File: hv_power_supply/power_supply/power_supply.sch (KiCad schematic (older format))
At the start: 0 parts

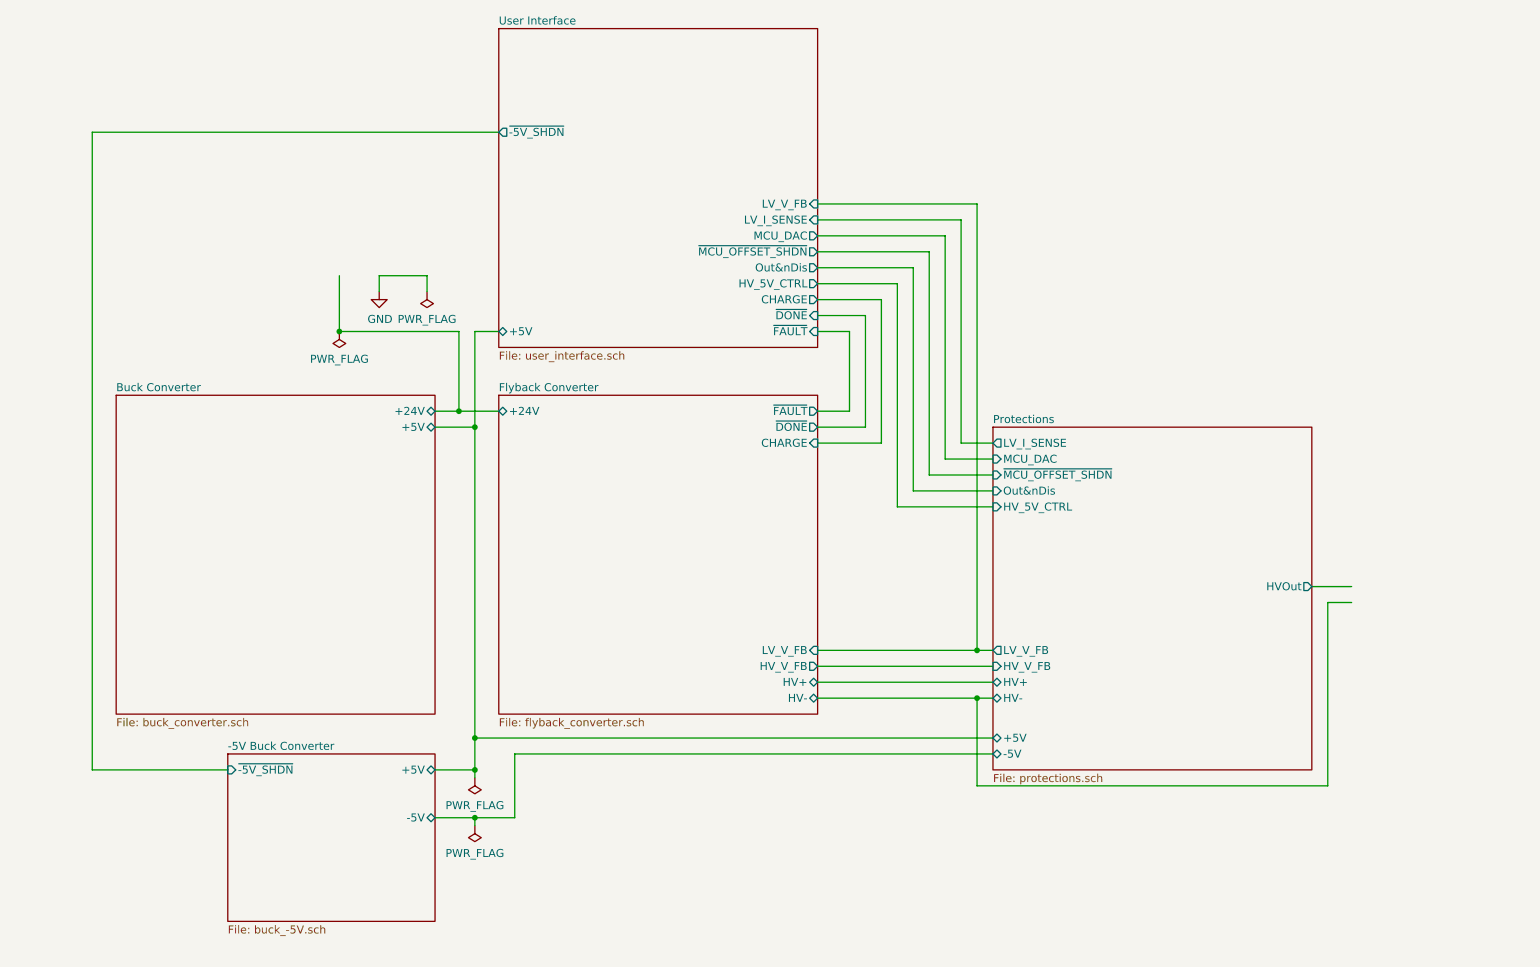
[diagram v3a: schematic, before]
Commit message: Fixed all component footprint issues, beginning to lay out flyback portion
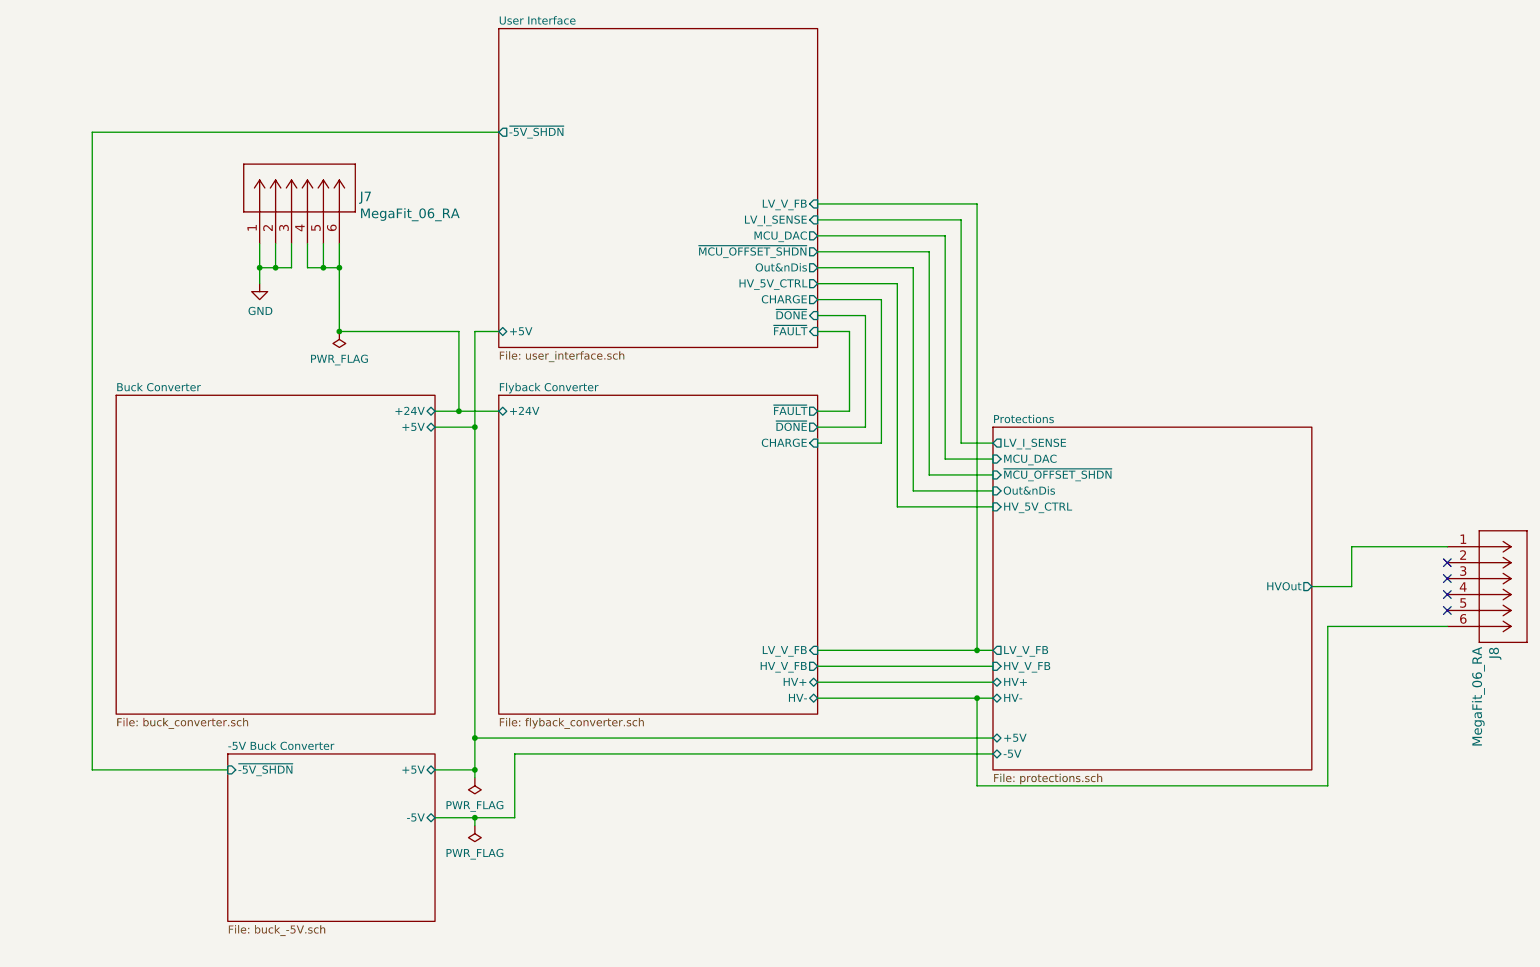
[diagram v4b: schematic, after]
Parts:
- added J7, J8: MegaFit_06_RA, footprints:MegaFit_06_RA, symbol formula:MegaFit_06_RA
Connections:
- wire segments 61 -> 71
- no-connect marks 0 -> 4
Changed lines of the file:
@@
 	7200 4950 7300 4950
-Wire Wire Line
-	9400 4350 9550 4350
 Wire Wire Line
 	9300 4250 9550 4250
@@
 L power:GND #PWR01
 U 1 1 607CC6CE
-P 3450 2400
-F 0 "#PWR01" H 3450 2150 50  0001 C CNN
-F 1 "GND" H 3455 2227 50  0000 C CNN
-F 2 "" H 3450 2400 50  0001 C CNN
-F 3 "" H 3450 2400 50  0001 C CNN
-	1    3450 2400
+P 2700 2350
+F 0 "#PWR01" H 2700 2100 50  0001 C CNN
+F 1 "GND" H 2705 2177 50  0000 C CNN
+F 2 "" H 2700 2350 50  0001 C CNN
+F 3 "" H 2700 2350 50  0001 C CNN
+	1    2700 2350
 	1    0    0    -1
 $EndComp
@@
 Connection ~ 3200 2650
 $Comp
-L power:PWR_FLAG #FLG02
+L power:PWR_FLAG #FLG03
 U 1 1 605FBEF3
 P 4050 5450
-F 0 "#FLG02" H 4050 5525 50  0001 C CNN
+F 0 "#FLG03" H 4050 5525 50  0001 C CNN
 F 1 "PWR_FLAG" H 4050 5623 50  0000 C CNN
 F 2 "" H 4050 5450 50  0001 C CNN
@@
 	4050 5400 4050 5450
 $Comp
-L power:PWR_FLAG #FLG03
+L power:PWR_FLAG #FLG04
 U 1 1 605FB304
 P 4050 5750
-F 0 "#FLG03" H 4050 5825 50  0001 C CNN
+F 0 "#FLG04" H 4050 5825 50  0001 C CNN
 F 1 "PWR_FLAG" H 4050 5923 50  0000 C CNN
 F 2 "" H 4050 5750 50  0001 C CNN
@@
 	7200 4950 7200 5500
 Wire Wire Line
-	9400 4350 9400 5500
-Wire Wire Line
 	4300 5700 4300 5300
 Wire Wire Line
 	4300 5300 7300 5300
-$Comp
-L power:PWR_FLAG #FLG0101
-U 1 1 6063E536
-P 3750 2400
-F 0 "#FLG0101" H 3750 2475 50  0001 C CNN
-F 1 "PWR_FLAG" H 3750 2573 50  0000 C CNN
-F 2 "" H 3750 2400 50  0001 C CNN
-F 3 "" H 3750 2400 50  0001 C CNN
-	1    3750 2400
-	-1   0    0    1
-$EndComp
-Wire Wire Line
-	3450 2400 3450 2300
-Wire Wire Line
-	3450 2300 3750 2300
-Wire Wire Line
-	3750 2300 3750 2400
-Wire Wire Line
-	3200 2300 3200 2650
+Wire Wire Line
+	2700 2350 2700 2250
 Wire Wire Line
 	6200 2250 6800 2250
@@
 Wire Wire Line
 	1650 1400 4200 1400
+$Comp
+L formula:MegaFit_06_RA J7
+U 1 1 60636060
+P 2700 2100
+F 0 "J7" V 2995 1472 60  0000 R CNN
+F 1 "MegaFit_06_RA" V 2889 1472 60  0000 R CNN
+F 2 "footprints:MegaFit_06_RA" H 3100 1840 60  0001 C CNN
+F 3 "https://www.molex.com/pdm_docs/as/AS-76823-100.pdf" H 2700 2100 60  0001 C CNN
+F 4 "https://www.digikey.com/en/products/detail/molex/0768250006/5639613" H 2700 2100 50  0001 C CNN "Purchasing Link"
+F 5 "Molex" H 2700 2100 50  0001 C CNN "MFN"
+F 6 "0768250006" H 2700 2100 50  0001 C CNN "MPN"
+	1    2700 2100
+	0    -1   -1   0
+$EndComp
+Wire Wire Line
+	2700 2250 2700 2100
+Connection ~ 2700 2250
+Wire Wire Line
+	2700 2250 2800 2250
+Wire Wire Line
+	2800 2250 2800 2100
+Wire Wire Line
+	2800 2250 2900 2250
+Wire Wire Line
+	2900 2250 2900 2100
+Connection ~ 2800 2250
+Wire Wire Line
+	3000 2100 3000 2250
+Wire Wire Line
+	3000 2250 3100 2250
+Wire Wire Line
+	3200 2250 3200 2650
+Wire Wire Line
+	3200 2100 3200 2250
+Connection ~ 3200 2250
+Wire Wire Line
+	3100 2100 3100 2250
+Connection ~ 3100 2250
+Wire Wire Line
+	3100 2250 3200 2250
+$Comp
+L formula:MegaFit_06_RA J8
+U 1 1 6064DEAA
+P 10150 4000
+F 0 "J8" V 10445 3372 60  0000 R CNN
+F 1 "MegaFit_06_RA" V 10339 3372 60  0000 R CNN
+F 2 "footprints:MegaFit_06_RA" H 10550 3740 60  0001 C CNN
+F 3 "https://www.molex.com/pdm_docs/as/AS-76823-100.pdf" H 10150 4000 60  0001 C CNN
+F 4 "https://www.digikey.com/en/products/detail/molex/0768250006/5639613" H 10150 4000 50  0001 C CNN "Purchasing Link"
+F 5 "Molex" H 10150 4000 50  0001 C CNN "MFN"
+F 6 "0768250006" H 10150 4000 50  0001 C CNN "MPN"
+	1    10150 4000
+	1    0    0    -1
+$EndComp
+Wire Wire Line
+	9550 4250 9550 4000
+Wire Wire Line
+	9550 4000 10150 4000
+Wire Wire Line
+	9400 4500 10150 4500
+Wire Wire Line
+	9400 4500 9400 5500
+NoConn ~ 10150 4400
+NoConn ~ 10150 4300
+NoConn ~ 10150 4200
+NoConn ~ 10150 4100
 $EndSCHEMATC
